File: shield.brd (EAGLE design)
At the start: 100 x 80.2 mm, 31 parts, among them Q1 PMV20EN, Q2 PMV20EN, Q3 PMV20EN, Q4 PMV20EN, Q5 PMV20EN, Q6 PMV20EN, U1 ATMEGA168

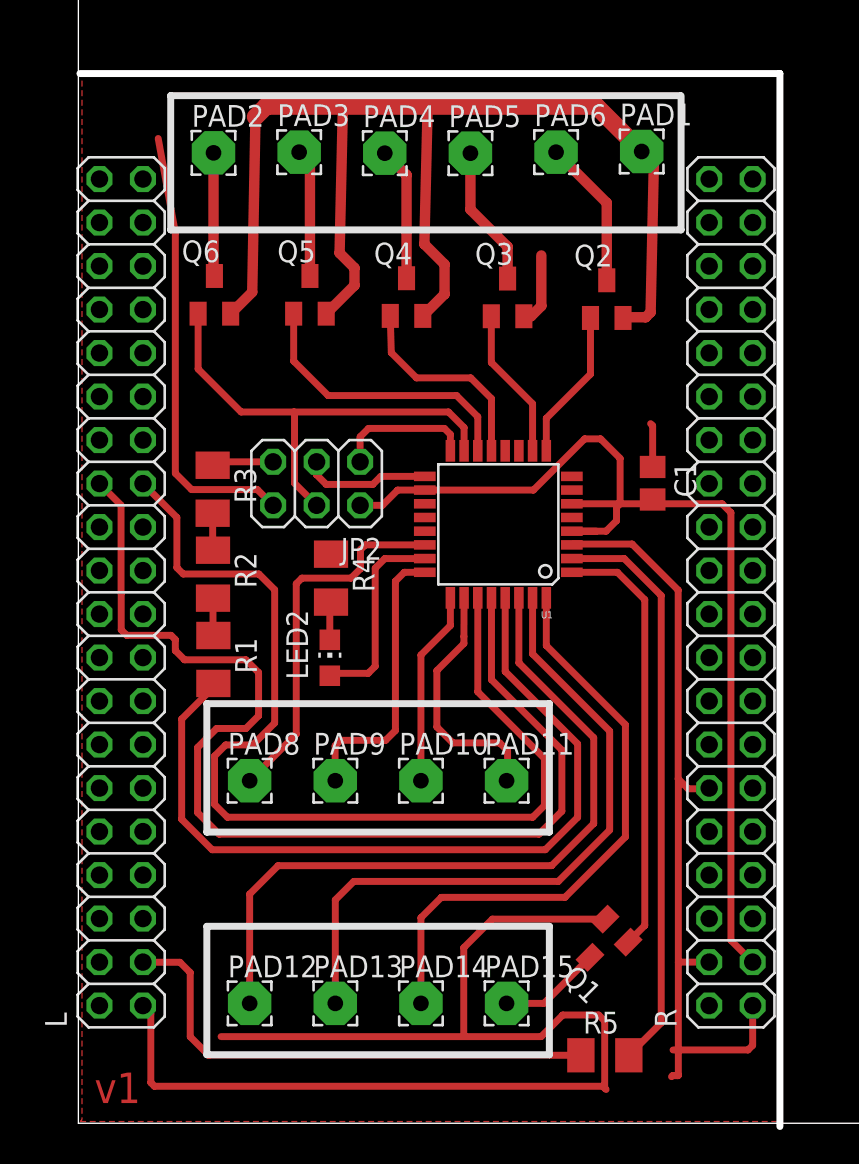
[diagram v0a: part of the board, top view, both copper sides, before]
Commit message: added 3.3/5V, a chargin pin and fixed chip layout
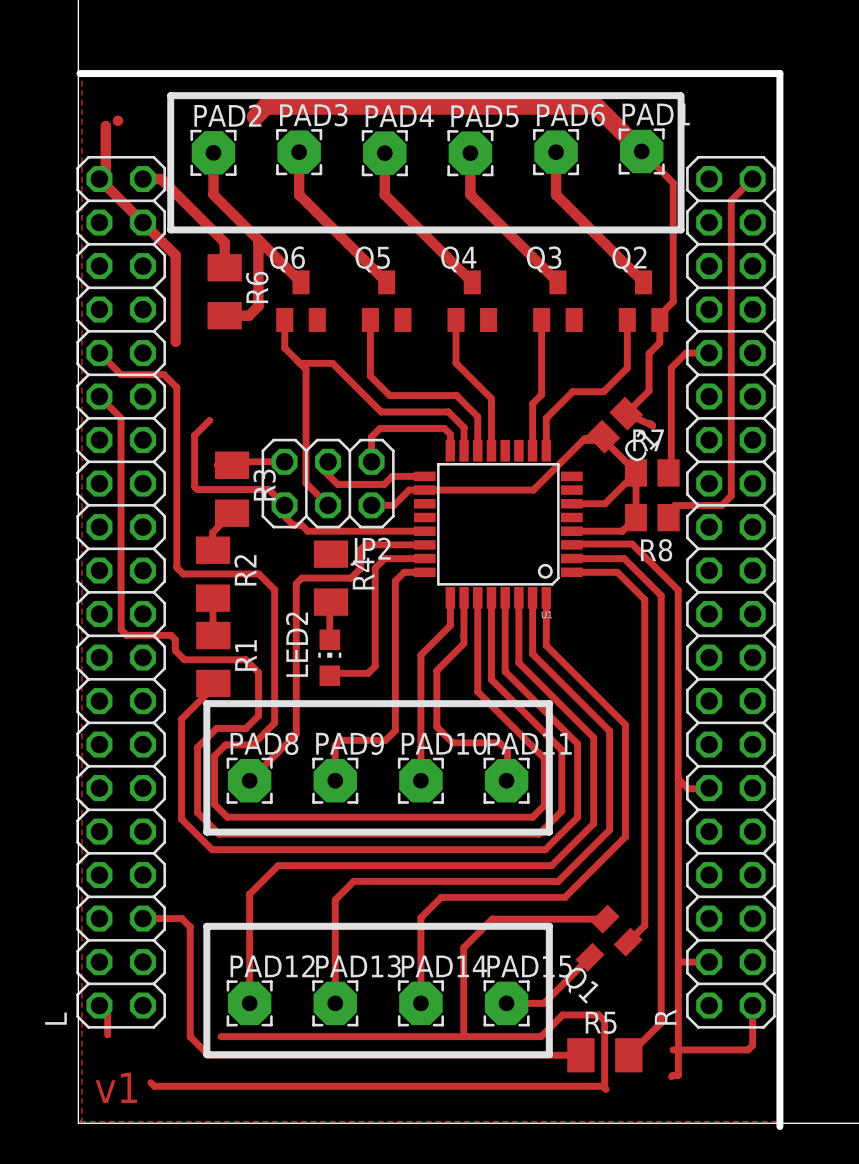
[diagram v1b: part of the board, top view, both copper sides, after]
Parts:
- added R6: (no value), rcl:M1206
- added R7, R8: (no value), rcl:M0805
- moved Q6 5.07 mm to (13.0, 48.0)
- moved Q5 4.50 mm to (18.0, 48.0)
- moved C1 4.05 mm to (31.3, 40.8), turned to 225 degrees
- moved Q4 3.85 mm to (23.0, 48.0)
- moved Q3 2.95 mm to (28.0, 48.0)
- moved Q2 2.15 mm to (33.0, 48.0)
- moved R3 1.13 mm to (8.97, 37.0)
- moved JP2 0.67 mm to (14.6, 37.4)
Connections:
- removed net N$20: R.40
- removed net N$22: L.2
- new net 3V3: R.32, R7.2
- new net VCC: C1.2, JP2.2, R7.1, R8.2, U1.18, U1.4, U1.6
- new net VIN: L.39, R6.1
- new net _1V8: L.34
- new net _3V3: L.36
- new net _5V: L.38
- net 5V: now also R.39, R8.1; no longer C1.2, JP2.2, R.3, U1.18, U1.4, U1.6
- net GND: now also L.2, L.37, R.40, U1.21; no longer L.1, L.39, R.39
- net N$25: now also L.5; no longer L.3
- net N$9: now also R6.2
- net SCK: now also L.30; no longer L.26
- net SDA: now also L.32; no longer L.25
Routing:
- net 5V: track 61.9 -> 23.3 mm
- net GND: track 227.0 -> 195.5 mm
- net VCC: track 0.00 -> 30.8 mm
- net SDA: track 60.5 -> 70.6 mm
- net 3V3: track 0.00 -> 8.77 mm
- net N$9: track 7.21 -> 15.8 mm
- net VIN: track 0.00 -> 7.78 mm
- net SCK: track 65.7 -> 70.7 mm
- net OC1_PWM2: track 16.9 -> 12.5 mm
- net OC1_PWM1: track 12.2 -> 8.49 mm
- net OC2_PWM2: track 27.5 -> 24.4 mm
- net N$25: track 30.0 -> 32.6 mm
- net N$8: track 7.49 -> 9.72 mm
- net N$7: track 7.83 -> 9.66 mm
- net OC0_PWM1: track 8.83 -> 10.7 mm
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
